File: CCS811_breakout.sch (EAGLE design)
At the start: 48 parts, among them J3 USB-MICROB, U1 ATMEGA328P, U10 CCS811, U11 RFM69HW, U2 TSL2561, U4 MPL115A, U5 FT231XS, U7 SHT31, U8 MCP1703/3.3V, U9 MCP1703CB, Y1 16MHZ

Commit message: Updated brd file
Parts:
- removed C1, C16, C17, C6: 1uF, SparkFun-Capacitors:CAP0805
- removed C11: 0.1uF, SparkFun-Capacitors:CAP0805
- removed C12, C13, C14, C15, C3, C4, C7: 0.1uF, SparkFun-Passives:CAP0805
- removed J2: (no value), SparkFun-Connectors:M05X2PTH
- removed J3: USB-MICROB, SparkFun-Connectors:USB-MICROB
- removed LED2: (no value), adafruit:LEDCHIPLED_0805
- removed MICS4514: SPARKFUN-SENSORS_MICS-4514, MICS-4514_CO_and_NOx_Sensor_Breakout:SPARKFUN-SENSORS_MICS-4514
- removed MOSFET: SPARKFUN-DISCRETESEMI_MOSFET-NCHANNELBSS138, MICS-4514_CO_and_NOx_Sensor_Breakout:SPARKFUN-DISCRETESEMI_MOSFET-NCHANNELBSS138
- removed R10, R9: 47, SparkFun-Passives:RESISTOR0805-RES
- removed R11: SHOTTKY, SparkFun-Passives:RESISTOR0805-RES
- removed R12, R21: 27, SparkFun-Passives:RESISTOR0805-RES
- removed R13: 10K, SparkFun-Passives:RESISTOR0805-RES
- removed R14: 47K, SparkFun-Passives:RESISTOR0805-RES
- removed R15, R18: 82, SparkFun-Passives:RESISTOR0805-RES
- removed R16: 22K, SparkFun-Passives:RESISTOR0805-RES
- removed R17: 51, SparkFun-Passives:RESISTOR0805-RES
- removed R19: 100K, SparkFun-Passives:RESISTOR0805-RES
- removed R20: 100, SparkFun-Passives:RESISTOR0805-RES
- removed R4: 47, SparkFun-Resistors:RESISTOR0805-RES
- removed R5, R6: 10K, SparkFun-Resistors:RESISTOR0805-RES
- removed RX: Green, adafruit:LEDCHIPLED_0805
- removed TX: Red, adafruit:LEDCHIPLED_0805
- removed U1: ATMEGA328P, SparkFun-DigitalIC:ATMEGA328P_TQFP
- removed U11: RFM69HW, RFM69 USB Gateway:LOWPOWERLAB_RFM69
- removed U2: TSL2561, SparkFun-DigitalIC:TSL2561FN
- removed U4: MPL115A, SparkFun-Sensors:MPL115A
- removed U5: FT231XS, SparkFun-DigitalIC:FT231XS
- removed U7: SHT31, thomasb9511:SHT31-DIS
- removed U8: MCP1703/3.3V, linear:MCP1703CB
- removed U9: MCP1703CB, linear:MCP1703CB
- removed X1: (no value), adafruit:SMACONNECTOR_EDGE
- removed Y1: 16MHZ, SparkFun-FreqCtrl:RESONATOR16MHZ
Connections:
- removed net 5V: C17.1, C7.1, MICS4514.RH2_OX, MICS4514.RH2_RED, MICS4514.RS2_OX, MICS4514.RS2_RED, U9.VO
- removed net A0: U1.PC0(ADC0)
- removed net A7: U1.ADC7
- removed net ANT: U11.ANT, X1.ANT
- removed net D2: U1.PD2(INT0), U11.DIO0
- removed net D5: U1.PD5(T1)
- removed net DTR: C12.1, J2.10, U5.!DTR
- removed net FTDI_VCC: R10.1, R9.1, U5.!RESET, U5.3V3OUT, U5.VCCIO
- removed net MISO: J2.1, U1.PB4(MISO), U11.MISO
- removed net MOSI: J2.4, U1.PB3(MOSI/OC2), U11.MOSI
- removed net N$12: C13.1, U4.CAP
- removed net N$13: MICS4514.RH1_RED, R15.2
- removed net N$17: RX.C, U5.CBUS1
- removed net N$18: TX.C, U5.CBUS2
- removed net N$2: R4.1, U1.PB1(OC1A)
- removed net N$20: MOSFET.D, R17.2, R18.1
- removed net N$23: MOSFET.G, R19.2, R20.1
- removed net N$25: R21.1, U5.USBDM
- removed net N$26: R12.1, U5.USBDP
- removed net N$27: R9.2, RX.A
- removed net N$29: R10.2, TX.A
- removed net N$3: LED2.A, R4.2
- removed net N$32: J3.D-, R21.2
- removed net N$33: J3.D+, R12.2
- removed net N$4: U1.PB7(XTAL2/TOSC2), Y1.3
- removed net N$5: U1.PB6(XTAL1/TOSC1), Y1.1
- removed net N$8: MICS4514.RH1_OX, R18.2
- removed net PRE: R20.2, U1.PD3(INT1)
- removed net PWR: C1.1, C16.1, J2.2, R11.1, U8.VI, U9.VI
- removed net RESET: C12.2, J2.5, R13.1, U1.PC6(/RESET)
- removed net RX: J2.7, U1.PD0(RXD), U5.TXD
- removed net SCK: J2.3, U1.PB5(SCK), U11.SCK
- removed net SS: U1.PB2(SS/OC1B), U11.SEL
- removed net TX: J2.8, U1.PD1(TXD), U5.RXD
- removed net VBUS: C11.1, J3.VBUS, R11.2, U5.VCC
- removed net VNOX: MICS4514.RS1_OX, R16.2, U1.PC1(ADC1)
- removed net VRED: MICS4514.RS1_RED, R14.2, U1.PC2(ADC2)
- net GND: no longer C1.2, C11.2, C13.2, C14.2, C15.2, C16.2, C17.2, C3.2, C4.2, C6.2, C7.2, J2.6, J3.GND, LED2.C, MOSFET.S, R14.1, R15.1, R16.1, R17.1, R19.1, U1.AGND, U1.GND@3, U1.GND@5, U11.GND, U2.GND, U4.GND, U5.GND@16, U5.GND@6, U7.ADDR, U7.GND, U7.NC, U8.GND, U9.GND, X1.GND1, X1.GND2, X1.GND3, X1.GND4, Y1.2
- net SCL: no longer R6.1, U1.PC5(ADC5/SCL), U2.SCL, U4.SCLK, U7.SCL
- net SDA: no longer R5.1, U1.PC4(ADC4/SDA), U2.SDA, U4.SDA/DIN, U7.SDA
- net VCC: no longer C14.1, C15.1, C3.1, C4.1, C6.1, R13.2, R5.2, R6.2, U1.AVCC, U1.VCC@4, U1.VCC@6, U11.VCC, U2.VDD, U4.SHDN, U4.VDD, U7.VCC, U8.VO
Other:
- note added: "Breakout"
- note added: "CCS811"
- note added: "Designed by Akram Ali"
- note added: "v0.1 (October 2016)"
- note removed: "0x39"
- note removed: "0x44"
- note removed: "0x60"
- note removed: "3.3V voltage regulator"
- note removed: "5V voltage regulator"
- note removed: "Air Pressure"
- note removed: "CO and NO2 concentration"
- note removed: "CRT Labs"
- note removed: "Designed by Akram Ali and Dave Conroy"
- note removed: "ISP"
- note removed: "Light Intensity"
- note removed: "RFM69HW"
- note removed: "Sensor Node"
- note removed: "Temperature and Relative Humidity"
- note removed: "USB + FTDI"
- note removed: "VOC and CO2"
- note removed: "v0.6 (October 2016)"
- moved on the sheet: C5, R2, U10

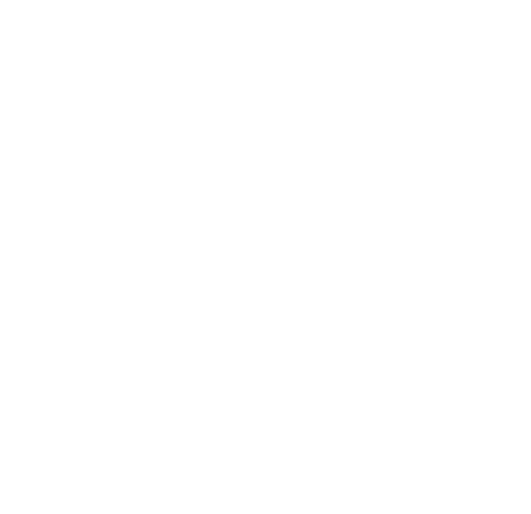
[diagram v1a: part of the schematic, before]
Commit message: Added 1x4 header
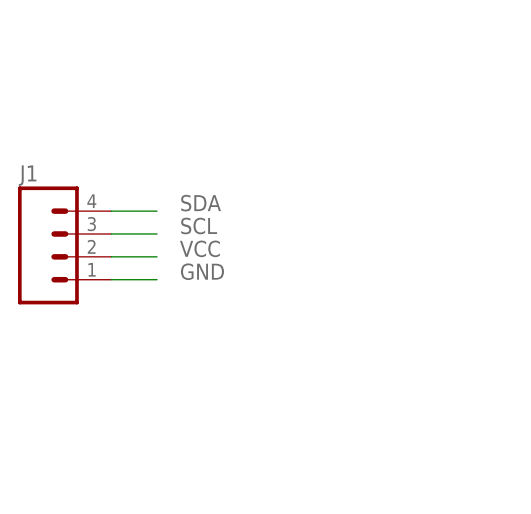
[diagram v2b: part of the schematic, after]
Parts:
- added J1: (no value), SparkFun-Connectors:M04PTH
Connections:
- net GND: now also J1.1
- net SCL: now also J1.3
- net SDA: now also J1.4
- net VCC: now also J1.2
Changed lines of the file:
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@@
 <layers>
 <layer number="1" name="Top" color="4" fill="1" visible="no" active="no"/>
+<layer number="2" name="Route2" color="1" fill="3" visible="no" active="no"/>
+<layer number="3" name="Route3" color="4" fill="3" visible="no" active="no"/>
+<layer number="4" name="Route4" color="1" fill="4" visible="no" active="no"/>
+<layer number="5" name="Route5" color="4" fill="4" visible="no" active="no"/>
+<layer number="6" name="Route6" color="1" fill="8" visible="no" active="no"/>
+<layer number="7" name="Route7" color="4" fill="8" visible="no" active="no"/>
+<layer number="8" name="Route8" color="1" fill="2" visible="no" active="no"/>
+<layer number="9" name="Route9" color="4" fill="2" visible="no" active="no"/>
+<layer number="10" name="Route10" color="1" fill="7" visible="no" active="no"/>
+<layer number="11" name="Route11" color="4" fill="7" visible="no" active="no"/>
+<layer number="12" name="Route12" color="1" fill="5" visible="no" active="no"/>
+<layer number="13" name="Route13" color="4" fill="5" visible="no" active="no"/>
+<layer number="14" name="Route14" color="1" fill="6" visible="no" active="no"/>
+<layer number="15" name="Route15" color="4" fill="6" visible="no" active="no"/>
 <layer number="16" name="Bottom" color="1" fill="1" visible="no" active="no"/>
 <layer number="17" name="Pads" color="2" fill="1" visible="no" active="no"/>
@@
 </part>
 <part name="SUPPLY10" library="SparkFun-Aesthetics" deviceset="VCC" device=""/>
+<part name="J1" library="SparkFun-Connectors" deviceset="M04" device="PTH"/>
 </parts>
 <sheets>
@@
 </instance>
 <instance part="SUPPLY10" gate="G$1" x="-27.94" y="55.88"/>
+<instance part="J1" gate="G$1" x="-109.22" y="35.56"/>
 </instances>
 <busses>
@@
 <label x="0" y="15.24" size="1.778" layer="95" rot="R270" xref="yes"/>
 </segment>
+<segment>
+<pinref part="J1" gate="G$1" pin="1"/>
+<wire x1="-104.14" y1="33.02" x2="-99.06" y2="33.02" width="0.1524" layer="91"/>
+<label x="-96.52" y="33.02" size="1.778" layer="95"/>
+</segment>
 </net>
 <net name="VCC" class="0">
@@
 <pinref part="SUPPLY10" gate="G$1" pin="VCC"/>
 </segment>
+<segment>
+<pinref part="J1" gate="G$1" pin="2"/>
+<wire x1="-104.14" y1="35.56" x2="-99.06" y2="35.56" width="0.1524" layer="91"/>
+<label x="-96.52" y="35.56" size="1.778" layer="95"/>
+</segment>
 </net>
 <net name="SCL" class="0">
@@
 <label x="25.4" y="43.18" size="1.778" layer="95" xref="yes"/>
 </segment>
+<segment>
+<pinref part="J1" gate="G$1" pin="3"/>
+<wire x1="-104.14" y1="38.1" x2="-99.06" y2="38.1" width="0.1524" layer="91"/>
+<label x="-96.52" y="38.1" size="1.778" layer="95"/>
+</segment>
 </net>
 <net name="SDA" class="0">
@@
 <label x="25.4" y="38.1" size="1.778" layer="95" xref="yes"/>
 </segment>
-</net>
+<segment>
+<pinref part="J1" gate="G$1" pin="4"/>
+<wire x1="-104.14" y1="40.64" x2="-99.06" y2="40.64" width="0.1524" layer="91"/>
+<label x="-96.52" y="40.64" size="1.778" layer="95"/>
+</segment>
+</net>

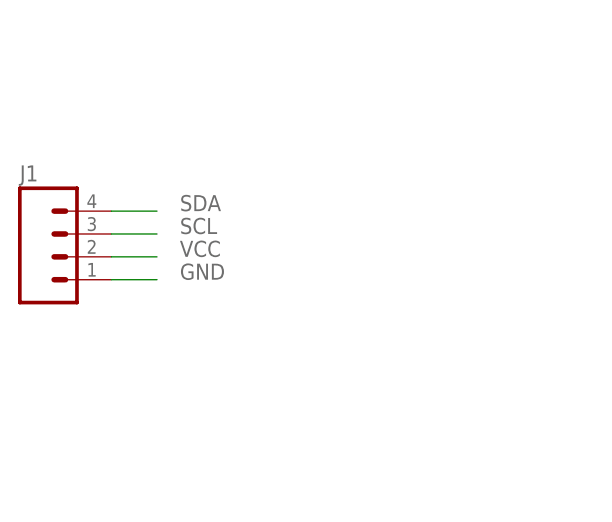
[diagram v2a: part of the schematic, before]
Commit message: Updated the board layout
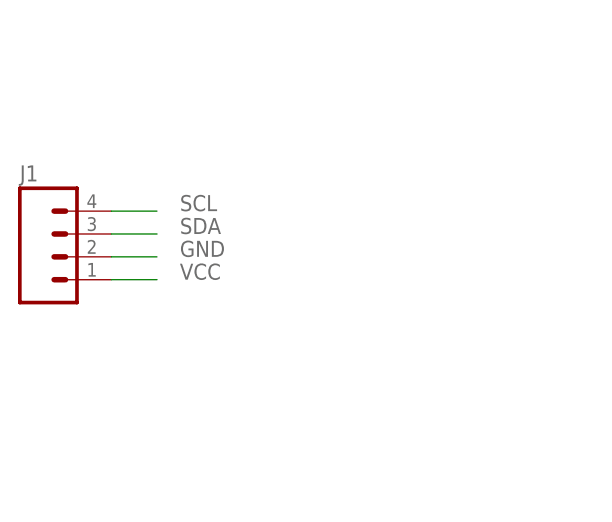
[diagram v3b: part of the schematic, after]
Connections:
- net GND: now also J1.2; no longer J1.1
- net SCL: now also J1.4; no longer J1.3
- net SDA: now also J1.3; no longer J1.4
- net VCC: now also J1.1; no longer J1.2
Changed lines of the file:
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@@
 </segment>
 <segment>
-<pinref part="J1" gate="G$1" pin="1"/>
-<wire x1="-104.14" y1="33.02" x2="-99.06" y2="33.02" width="0.1524" layer="91"/>
-<label x="-96.52" y="33.02" size="1.778" layer="95"/>
+<pinref part="J1" gate="G$1" pin="2"/>
+<wire x1="-104.14" y1="35.56" x2="-99.06" y2="35.56" width="0.1524" layer="91"/>
+<label x="-96.52" y="35.56" size="1.778" layer="95"/>
 </segment>
 </net>
@@
 </segment>
 <segment>
-<pinref part="J1" gate="G$1" pin="2"/>
-<wire x1="-104.14" y1="35.56" x2="-99.06" y2="35.56" width="0.1524" layer="91"/>
-<label x="-96.52" y="35.56" size="1.778" layer="95"/>
+<pinref part="J1" gate="G$1" pin="1"/>
+<wire x1="-104.14" y1="33.02" x2="-99.06" y2="33.02" width="0.1524" layer="91"/>
+<label x="-96.52" y="33.02" size="1.778" layer="95"/>
 </segment>
 </net>
@@
 </segment>
 <segment>
-<pinref part="J1" gate="G$1" pin="3"/>
-<wire x1="-104.14" y1="38.1" x2="-99.06" y2="38.1" width="0.1524" layer="91"/>
-<label x="-96.52" y="38.1" size="1.778" layer="95"/>
+<pinref part="J1" gate="G$1" pin="4"/>
+<wire x1="-104.14" y1="40.64" x2="-99.06" y2="40.64" width="0.1524" layer="91"/>
+<label x="-96.52" y="40.64" size="1.778" layer="95"/>
 </segment>
 </net>
@@
 </segment>
 <segment>
-<pinref part="J1" gate="G$1" pin="4"/>
-<wire x1="-104.14" y1="40.64" x2="-99.06" y2="40.64" width="0.1524" layer="91"/>
-<label x="-96.52" y="40.64" size="1.778" layer="95"/>
+<pinref part="J1" gate="G$1" pin="3"/>
+<wire x1="-104.14" y1="38.1" x2="-99.06" y2="38.1" width="0.1524" layer="91"/>
+<label x="-96.52" y="38.1" size="1.778" layer="95"/>
 </segment>
 </net>

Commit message: Updated schematic
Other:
- note added: "Designed by AKstudios http://github.com/AKstudios"
- note removed: "Designed by Akram Ali"
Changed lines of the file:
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@@
 (October 2016)</text>
 <text x="0" y="-45.72" size="1.27" layer="94" font="vector" ratio="10" align="bottom-center">Designed by
-Akram Ali</text>
+AKstudios
+http://github.com/AKstudios</text>
 <text x="7.62" y="22.86" size="1.778" layer="97">0x5B</text>
 </plain>

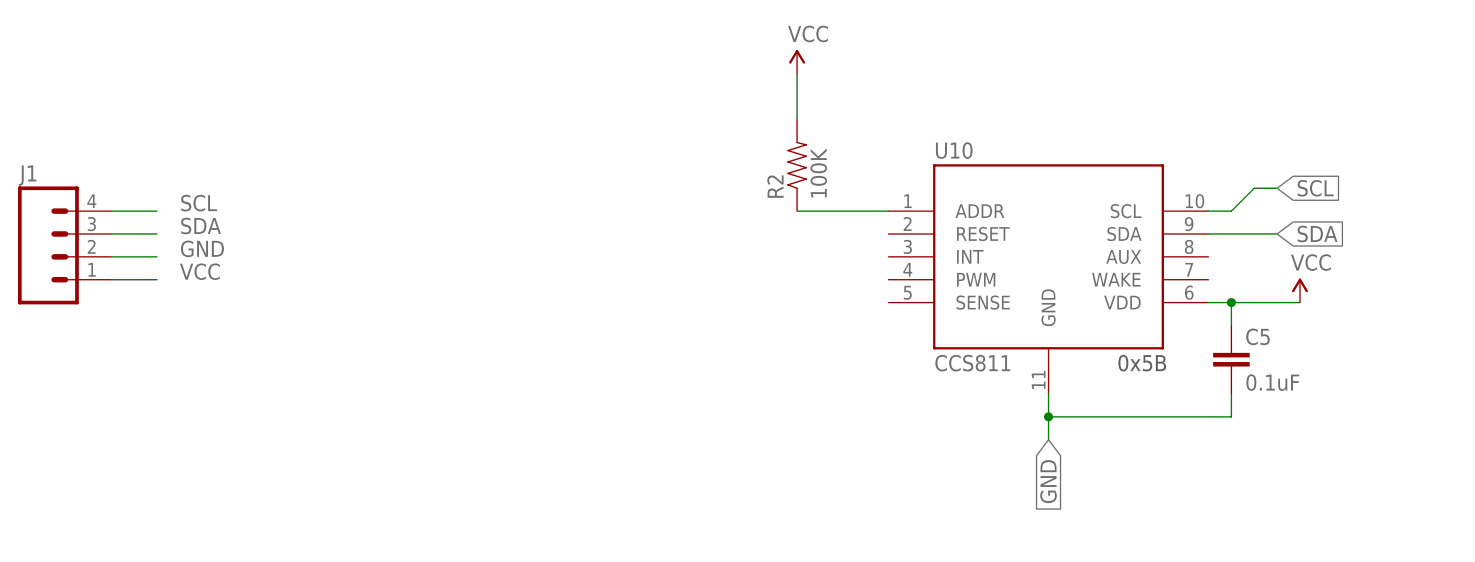
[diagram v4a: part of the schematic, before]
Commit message: Broken essential pins out
INT and WAKE pins are now broken out
Updated capacitor to 1uF as recommended by datasheet
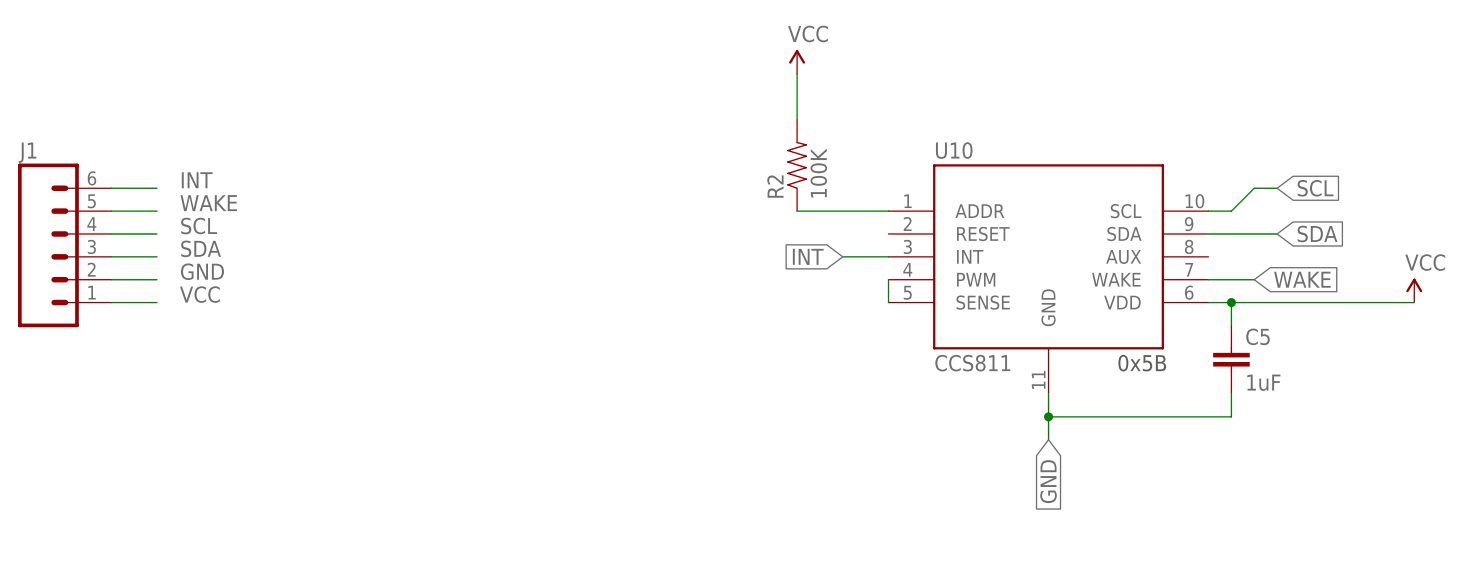
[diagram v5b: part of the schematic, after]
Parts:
- C5: value 0.1uF -> 1uF
- J1: device SparkFun-Connectors:M04PTH -> SparkFun-Connectors:M06SILK_FEMALE_PTH
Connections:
- new net INT: J1.6, U10.INT
- new net N$2: U10.PWM, U10.SENSE
- new net WAKE: J1.5, U10.WAKE
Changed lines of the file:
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@@
 <parts>
 <part name="U10" library="CCS811" deviceset="CCS811" device="-I2C" value="CCS811"/>
-<part name="C5" library="SparkFun-Passives" deviceset="CAP" device="0805" value="0.1uF">
+<part name="C5" library="SparkFun-Passives" deviceset="CAP" device="0805" value="1uF">
 <attribute name="MF" value=""/>
 <attribute name="MPN" value=""/>
@@
 </part>
 <part name="SUPPLY10" library="SparkFun-Aesthetics" deviceset="VCC" device=""/>
-<part name="J1" library="SparkFun-Connectors" deviceset="M04" device="PTH"/>
+<part name="J1" library="SparkFun-Connectors" deviceset="M06" device="SILK_FEMALE_PTH"/>
 </parts>
 <sheets>
@@
 <attribute name="MPN" x="20.32" y="22.86" size="1.778" layer="96" rot="R270" display="off"/>
 </instance>
-<instance part="SUPPLY5" gate="G$1" x="27.94" y="30.48"/>
+<instance part="SUPPLY5" gate="G$1" x="40.64" y="30.48"/>
 <instance part="R2" gate="G$1" x="-27.94" y="45.72" rot="R90">
 <attribute name="OC_NEWARK" x="-27.94" y="45.72" size="1.778" layer="96" display="off"/>
@@
 <segment>
 <pinref part="J1" gate="G$1" pin="2"/>
-<wire x1="-104.14" y1="35.56" x2="-99.06" y2="35.56" width="0.1524" layer="91"/>
-<label x="-96.52" y="35.56" size="1.778" layer="95"/>
+<wire x1="-104.14" y1="33.02" x2="-99.06" y2="33.02" width="0.1524" layer="91"/>
+<label x="-96.52" y="33.02" size="1.778" layer="95"/>
 </segment>
 </net>
@@
 <pinref part="C5" gate="G$1" pin="1"/>
 <pinref part="SUPPLY5" gate="G$1" pin="VCC"/>
-<wire x1="20.32" y1="30.48" x2="27.94" y2="30.48" width="0.1524" layer="91"/>
+<wire x1="20.32" y1="30.48" x2="40.64" y2="30.48" width="0.1524" layer="91"/>
 </segment>
 <segment>
@@
 <segment>
 <pinref part="J1" gate="G$1" pin="1"/>
-<wire x1="-104.14" y1="33.02" x2="-99.06" y2="33.02" width="0.1524" layer="91"/>
-<label x="-96.52" y="33.02" size="1.778" layer="95"/>
+<wire x1="-104.14" y1="30.48" x2="-99.06" y2="30.48" width="0.1524" layer="91"/>
+<label x="-96.52" y="30.48" size="1.778" layer="95"/>
 </segment>
 </net>
@@
 <segment>
 <pinref part="J1" gate="G$1" pin="4"/>
-<wire x1="-104.14" y1="40.64" x2="-99.06" y2="40.64" width="0.1524" layer="91"/>
-<label x="-96.52" y="40.64" size="1.778" layer="95"/>
+<wire x1="-104.14" y1="38.1" x2="-99.06" y2="38.1" width="0.1524" layer="91"/>
+<label x="-96.52" y="38.1" size="1.778" layer="95"/>
 </segment>
 </net>
@@
 <segment>
 <pinref part="J1" gate="G$1" pin="3"/>
-<wire x1="-104.14" y1="38.1" x2="-99.06" y2="38.1" width="0.1524" layer="91"/>
-<label x="-96.52" y="38.1" size="1.778" layer="95"/>
+<wire x1="-104.14" y1="35.56" x2="-99.06" y2="35.56" width="0.1524" layer="91"/>
+<label x="-96.52" y="35.56" size="1.778" layer="95"/>
 </segment>
 </net>
@@
 </segment>
 </net>
+<net name="WAKE" class="0">
+<segment>
+<pinref part="J1" gate="G$1" pin="5"/>
+<wire x1="-104.14" y1="40.64" x2="-99.06" y2="40.64" width="0.1524" layer="91"/>
+<label x="-96.52" y="40.64" size="1.778" layer="95"/>
+</segment>
+<segment>
+<pinref part="U10" gate="G$1" pin="WAKE"/>
+<wire x1="17.78" y1="33.02" x2="22.86" y2="33.02" width="0.1524" layer="91"/>
+<label x="22.86" y="33.02" size="1.778" layer="95" xref="yes"/>
+</segment>
+</net>
+<net name="INT" class="0">
+<segment>
+<pinref part="J1" gate="G$1" pin="6"/>
+<wire x1="-104.14" y1="43.18" x2="-99.06" y2="43.18" width="0.1524" layer="91"/>
+<label x="-96.52" y="43.18" size="1.778" layer="95"/>
+</segment>
+<segment>
+<pinref part="U10" gate="G$1" pin="INT"/>
+<wire x1="-17.78" y1="35.56" x2="-22.86" y2="35.56" width="0.1524" layer="91"/>
+<label x="-22.86" y="35.56" size="1.778" layer="95" rot="R180" xref="yes"/>
+</segment>
+</net>
+<net name="N$2" class="0">
+<segment>
+<pinref part="U10" gate="G$1" pin="SENSE"/>
+<pinref part="U10" gate="G$1" pin="PWM"/>
+<wire x1="-17.78" y1="30.48" x2="-17.78" y2="33.02" width="0.1524" layer="91"/>
+</segment>
+</net>
